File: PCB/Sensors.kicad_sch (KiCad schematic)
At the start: 6 parts, among them U2 BMI088, U5 BMP390

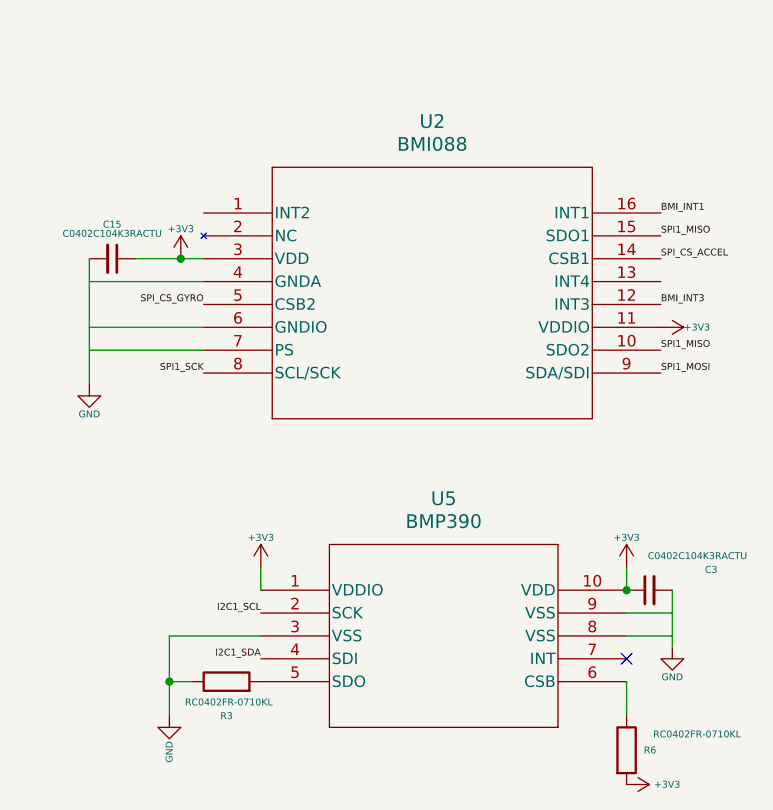
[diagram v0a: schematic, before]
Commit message: Sensors rework: ICM-42688-P + DPS310 replace BMI088/BMP390
- Full sensor-area rebuild per TDK DS-000347 + Infineon DPS310 datasheets
- ICM-42688-P on SPI1 (PC4 CS pending hierarchy), INT1/INT2, 100nF+2.2uF on VDD, 10nF on VDDIO, RESV to GND
- DPS310 on I2C1 (0x76 via SDO pull-down, INT capable), CSB to VDDIO, 100nF on VDD/VDDIO
- Working 2.2k I2C pull-ups to 3V3; all shorts (VSS/VDDIO rails) removed
- New project libs: OpenVCU.kicad_sym, OpenVCU.pretty (both footprints), sym/fp-lib-tables
- ERC Sensors: 28 errors -> 3 expected pre-hierarchy (undriven SPI inputs)
- BOM + README updated; datasheets archived under docs/
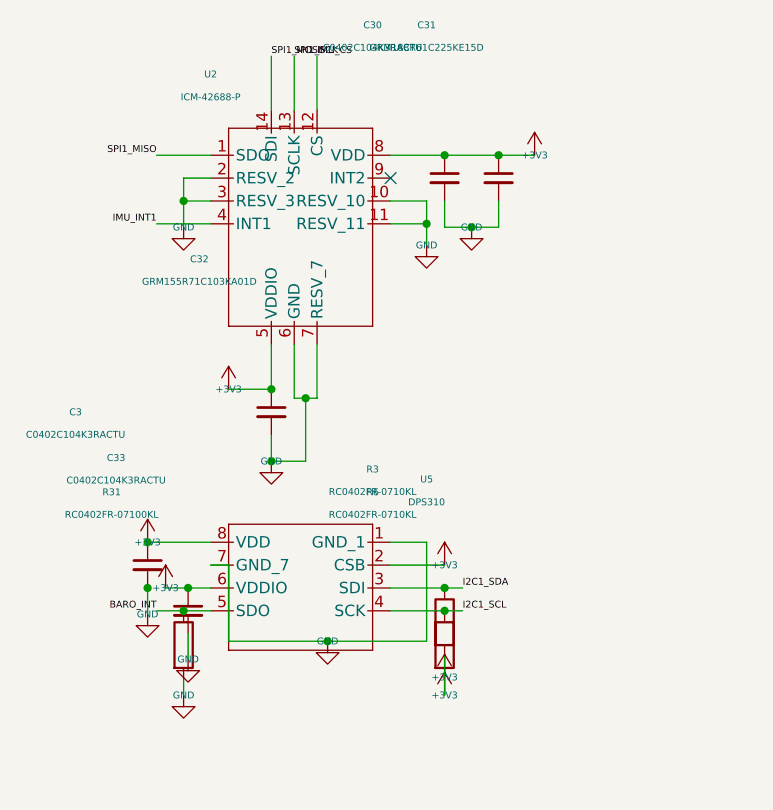
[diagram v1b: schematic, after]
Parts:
- removed C15: C0402C104K3RACTU, C0402C104K3RACTU:CAPC1005X55N, symbol Device:C_Small
- removed U2: BMI088, BMI088:QFN_BMI085_BOS, symbol 2026-03-01_16-46-43:BMI088
- removed U5: BMP390, BMP390:10LGA_2X2X0p75_BOS, symbol 2026-03-02_15-36-50:BMP390
- added C30, C33: C0402C104K3RACTU, C0402C104K3RACTU:CAPC1005X55N, symbol Device:C_Small
- added C31: GRM188R61C225KE15D, GRM188R61C225KE15D:CAPC1608X90N, symbol Device:C_Small
- added C32: GRM155R71C103KA01D, GRM155R71C103KA01D:CAPC1005X55N, symbol Device:C_Small
- added R31: RC0402FR-07100KL, RC0402FR-07100KL:RESC1005X40, symbol Device:R
- added U2: ICM-42688-P, OpenVCU:ICM-42688-P, symbol OpenVCU:ICM-42688-P
- added U5: DPS310, OpenVCU:DPS310, symbol OpenVCU:DPS310
- C3: Availability In Stock -> (none); Check_prices https://www.snapeda.com/parts/C0402C104K3RACTU/Kemet/view-p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 -> (none); Description_1 0.1 µF ±10% 25V Ceramic Capacitor X7R 0402 (1005 Metric) -> (none); MANUFACTURER KEMET -> (none); MAXIMUM_PACKAGE_HEIGHT 0.55mm -> (none); MF KEMET -> (none); MP C0402C104K3RACTU -> (none); PARTREV N/A -> (none); Package 402-2 KEMET -> (none); Price None -> (none); STANDARD IPC 7351B -> (none); SnapEDA_Link https://www.snapeda.com/parts/C0402C104K3RACTU/Kemet/view-p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 -> (none)
- R3, R6: Availability In Stock -> (none); Check_prices https://www.snapeda.com/parts/RC0402FR-0710KL/Yageo/view-pa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 -> (none); Description_1 10 kOhms ±1% 0.063W, 1/16W Chip Resistor 0402 (1005 Metric)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 -> (none); MANUFACTURER Yageo -> (none); MAXIMUM_PACKAGE_HEIGHT 0.4 mm -> (none); MF Yageo -> (none); MP RC0402FR-0710KL -> (none); PARTREV V.12 -> (none); Package 0402 Yageo -> (none); Price None -> (none); Purchase-URL https://www.snapeda.com/api/url_track_click_mouser/?unipart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 -> (none); SNAPEDA_PACKAGE_ID 7028 -> (none); STANDARD IPC 7351B -> (none); SnapEDA_Link https://www.snapeda.com/parts/RC0402FR-0710KL/Yageo/view-pa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 -> (none)
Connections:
- net +3V3: now also R3.2, C30.1, C31.1, C32.1, C33.1, U2.5 (VDDIO), U2.8 (VDD), U5.2 (CSB), U5.6 (VDDIO), U5.8 (VDD)
- net GND: now also C30.2, C31.2, C32.2, C33.2, R31.2, U2.10 (RESV_10), U2.11 (RESV_11), U2.2 (RESV_2), U2.3 (RESV_3), U2.6 (GND), U2.7 (RESV_7), U5.1 (GND_1), U5.7 (GND_7); no longer R3.1
- net I2C1_SCL: now also R6.1, U5.4 (SCK)
- net I2C1_SDA: now also R3.1, U5.3 (SDI)
- net SPI1_MISO: now also U2.1 (SDO)
- net SPI1_MOSI: now also U2.14 (SDI)
- net SPI1_SCK: now also U2.13 (SCLK)
- new net BARO_INT: R31.1, U5.5 (SDO)
- new net IMU_CS: U2.12 (CS)
- new net IMU_INT1: U2.4 (INT1)

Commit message: Power sheet P2: USB-C fix, buck replacement, LDO rewire, battery sense, pull-downs
- Replaced MP1584 buck with TPS54360 (EOL fix)
- Fixed USB-C: CC pull-downs, ESD wiring, VBUS path, shell ground
- Rewired LDO: VIN<-+5V, GND->GND, VOUT->+3V3, caps at pins
- Added battery sense divider (100k/10k from VBAT)
- Added SBU1/SBU2 1M pull-downs (R38, R39)
- Fixed component rotations for distinct pin tips (90°)
- Added PWR_FLAGS on +5V rail (source) and VBUS net
- Added SBU1/SBU2 1M pull-downs (R38, R39)
- Removed old MP1584 debris
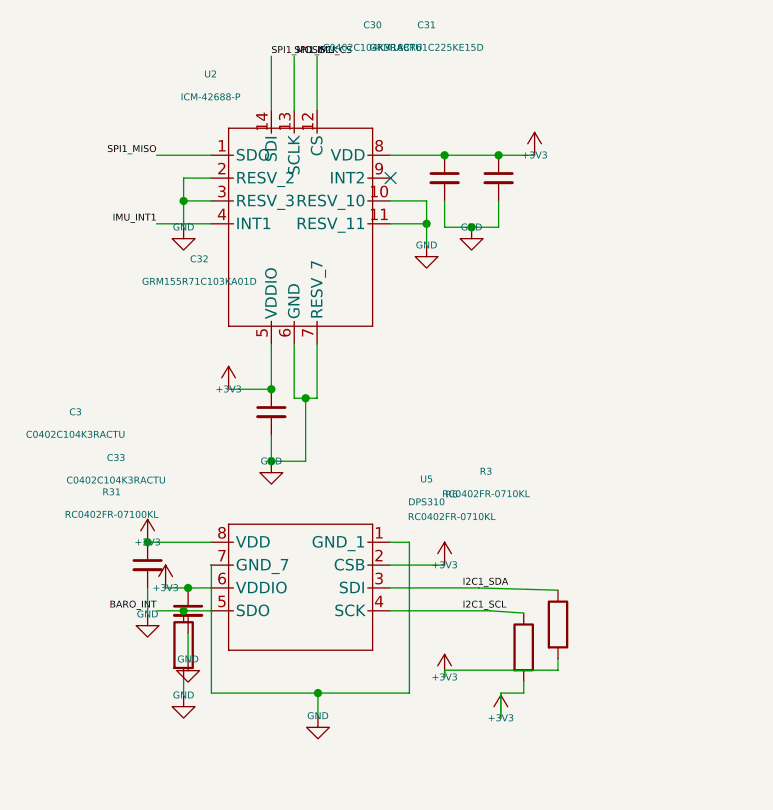
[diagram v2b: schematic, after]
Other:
- moved on the sheet: R3, R6

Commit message: Hierarchy: Sensors sheet hierarchical labels + root sheet pins (via Konnect)
- Added 8 hierarchical labels to Sensors.kicad_sch
- Fixed net-name mismatch: IMU_CS->SPI_CS_ACCEL, IMU_INT1->BMI_INT1 (match root MCU labels)
- Imported matching sheet pins on root Sensors instance
- validate_sheet_pins: 0 issues
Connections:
- net IMU_CS renamed SPI_CS_ACCEL
- net IMU_INT1 renamed BMI_INT1

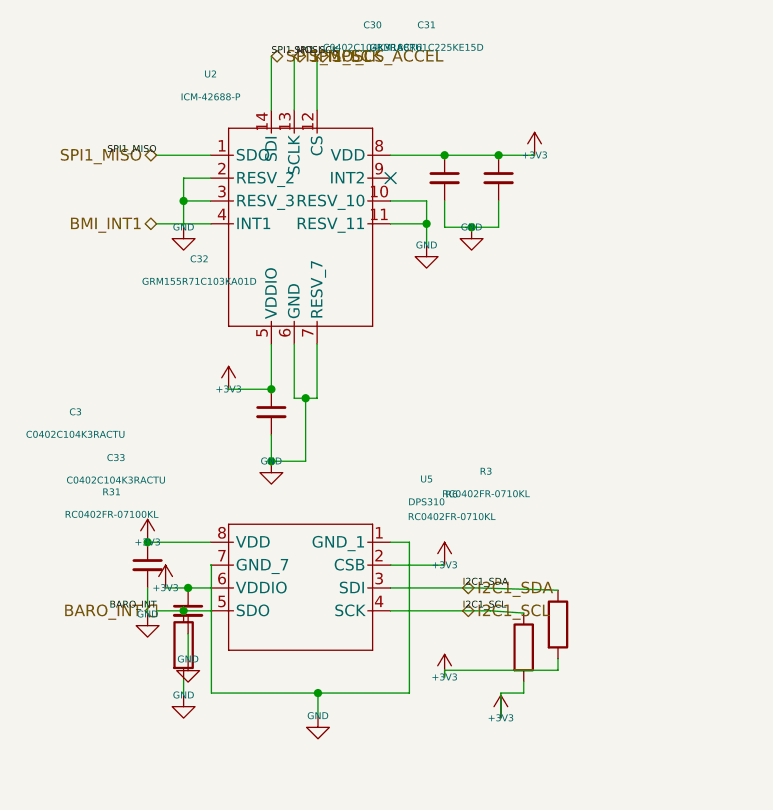
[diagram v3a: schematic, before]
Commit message: Sensors: put the sheet on the 1.27mm grid (project symbols only)
OpenVCU:ICM-42688-P and OpenVCU:DPS310 (the project's own symbols) had side
pins anchored at -8/-5.46/-2.92/-0.38 and -5/-2.46/0.08/2.62.  No pin was ever
a 1.27mm multiple, and because the pitches were 2.54 the error accumulated down
the side, so *no* instance translation could ever align them - every pin and
every wire on the sheet was permanently off-grid.

Only those two symbol definitions are changed: their pins now sit on a 2.54
pitch anchored on-grid, with the GND/RESV groups stacked onto one connection
point per device.  PCB/OpenVCU.kicad_sym is updated to match, and the sheet is
re-laid out on the grid.

Netlist is preserved: U2/U5/C3/C30-33/R31 and the I2C1 pull-ups R3/R6 all keep
their pins on the same nets as before (only R3/R6 pin numbers swap, which is
electrically identical for a resistor).

endpoint_off_grid: 64 -> 0.
ERC: 0 errors, 201 -> 91 warnings.

Note: the remaining 91 warnings are all vendor parts (ST, Murata, etc.) whose
symbol/footprint references point at private libraries that do not exist in
this environment; they are out of scope.
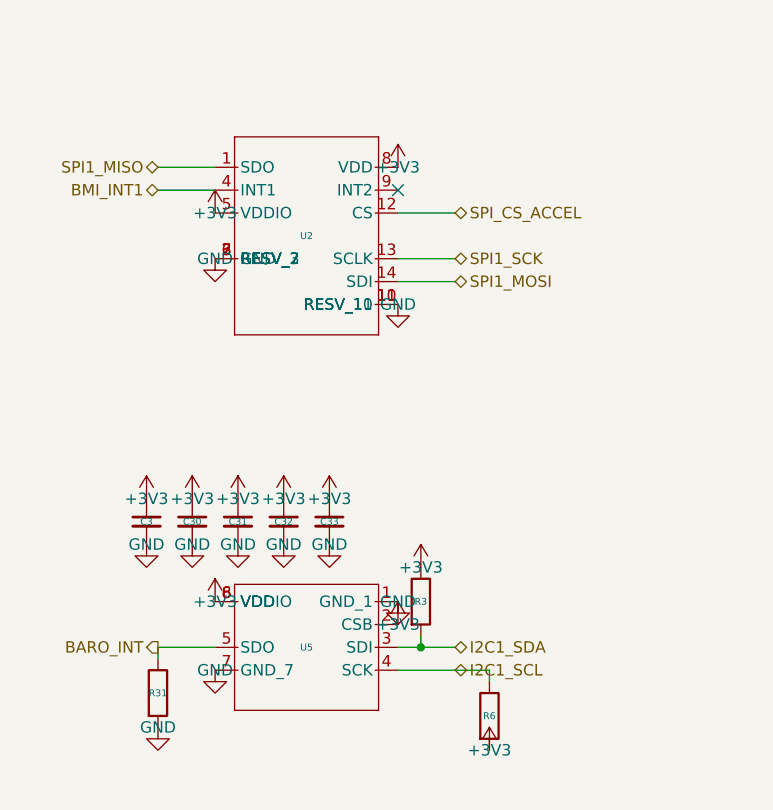
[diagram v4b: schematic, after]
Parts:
- C3, C30, C33: value C0402C104K3RACTU -> 100nF; footprint C0402C104K3RACTU:CAPC1005X55N -> Capacitor_SMD:C_0402_1005Metric
- C31: value GRM188R61C225KE15D -> 100nF; footprint GRM188R61C225KE15D:CAPC1608X90N -> Capacitor_SMD:C_0402_1005Metric
- C32: value GRM155R71C103KA01D -> 100nF; footprint GRM155R71C103KA01D:CAPC1005X55N -> Capacitor_SMD:C_0402_1005Metric
- R3, R6: value RC0402FR-0710KL -> 4.7k; footprint RC0402FR-0710KL:RESC1005X40N -> Resistor_SMD:R_0402_1005Metric
- R31: value RC0402FR-07100KL -> 100k; footprint RC0402FR-07100KL:RESC1005X40 -> Resistor_SMD:R_0402_1005Metric
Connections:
- net +3V3: now also R3.1; no longer R3.2
- net I2C1_SDA: now also R3.2; no longer R3.1
